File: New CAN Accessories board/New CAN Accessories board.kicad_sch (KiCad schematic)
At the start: 85 parts, among them J1 39301040, J10 39301040, J11 ATF13-2P-BM03, J2 39301040, J3 39301040, J4 39301040, J5 39301040, J6 39301040, J7 39301040, J8 39301040, J9 39301060, Q1 IRLML6344TRPBF, Q2 IRLML6344TRPBF, Q3 IRLML6344TRPBF, Q4 IRLML6344TRPBF, Q5 IRLML6344TRPBF, Q6 IRLML6344TRPBF, Q7 IRLML6344TRPBF, Q8 IRLML6344TRPBF, T1 MCP2562FD-E_SN, U1 NUCLEO_L432KC

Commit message: Annotate
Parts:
- renumbered Rterm to Rterm1, SWsel to SWsel1, SWtel to SWtel1
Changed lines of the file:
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@@
 		(on_board yes)
 		(dnp no)
-		(property "Reference" "Rterm"
+		(property "Reference" "Rterm1"
 			(at 44.958 144.8816 0)
 			(effects
@@
 			(project "New CAN Accessories board"
 				(path "/88340f43-3f46-45a6-9393-130e00dc3071"
-					(reference "Rterm")
+					(reference "Rterm1")
 					(unit 1)
 				)
@@
 		(dnp no)
 		(fields_autoplaced yes)
-		(property "Reference" "SWsel"
+		(property "Reference" "SWsel1"
 			(at 49.53 190.5 0)
 			(effects
@@
 			(project "New CAN Accessories board"
 				(path "/88340f43-3f46-45a6-9393-130e00dc3071"
-					(reference "SWsel")
+					(reference "SWsel1")
 					(unit 2)
 				)
@@
 		(dnp no)
 		(fields_autoplaced yes)
-		(property "Reference" "SWsel"
+		(property "Reference" "SWsel1"
 			(at 49.53 181.61 0)
 			(effects
@@
 			(project ""
 				(path "/88340f43-3f46-45a6-9393-130e00dc3071"
-					(reference "SWsel")
+					(reference "SWsel1")
 					(unit 1)
 				)
@@
 		(dnp no)
 		(fields_autoplaced yes)
-		(property "Reference" "SWtel"
+		(property "Reference" "SWtel1"
 			(at 87.63 190.5 0)
 			(effects
@@
 			(project "New CAN Accessories board"
 				(path "/88340f43-3f46-45a6-9393-130e00dc3071"
-					(reference "SWtel")
+					(reference "SWtel1")
 					(unit 2)
 				)
@@
 		(dnp no)
 		(fields_autoplaced yes)
-		(property "Reference" "SWtel"
+		(property "Reference" "SWtel1"
 			(at 87.63 181.61 0)
 			(effects
@@
 			(project "New CAN Accessories board"
 				(path "/88340f43-3f46-45a6-9393-130e00dc3071"
-					(reference "SWtel")
+					(reference "SWtel1")
 					(unit 1)
 				)

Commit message: preliminary layout complete
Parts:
- removed Cop1, Cop2, Cop3, Cop4, Cop5, Cop6, Cop7, Cop8: 100nF, Capacitor_SMD:C_0805_2012Metric, symbol Device:C
- removed D1, D2, D3, D4, D5, D6, D7, D8: LED, LED_SMD:LED_0805_2012Metric, symbol Device:LED
- removed F1, F2, F3, F4, F5, F6, F7, F8: Fuse, footprint:3586KTR, symbol Device:Fuse
- removed J1, J2, J3, J4, J5, J6, J7, J8: 39301040, Connector_Molex:Molex_Mini-Fit_Jr_5569-04A2_2x02_P4.20mm_Horizontal, symbol Connector_Generic:Conn_02x02_Top_Bottom
- removed OP1, OP2, OP3, OP4, OP5, OP6, OP7, OP8: MCP6C02T-020E/CHY, footprint:SOT-23-6_CHY_MCH-M, symbol sym:MCP6C02T-020E_CHY
- removed Q1, Q2, Q3, Q4, Q5, Q6, Q7, Q8: IRLML6344TRPBF, footprint:TRANS_IRLML6344TRPBF, symbol sym:IRLML6344TRPBF
- removed Rled1, Rled2, Rled3, Rled4, Rled5, Rled6, Rled7, Rled8: 100, Resistor_SMD:R_0805_2012Metric, symbol Device:R
- removed Rpd1, Rpd2, Rpd3, Rpd4, Rpd5, Rpd6, Rpd7, Rpd8: 10K, Resistor_SMD:R_0805_2012Metric, symbol Device:R
- removed Rsh1, Rsh2, Rsh3, Rsh4, Rsh5, Rsh6, Rsh7, Rsh8: 0.05, Resistor_SMD:R_2512_6332Metric_Pad1.40x3.35mm_HandSolder, symbol Device:R
- Rpd10, SWtel1: now not fitted
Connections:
- net BOARD_SW: now also SWsel1.6 (C), U1.PB3 (D13); no longer SWsel1.4 (A), U1.PB0 (D3)
- net CANRX: now also U1.PA9 (D1); no longer U1.PA11 (D10)
- net GATE1: now also U1.PB4 (D12); no longer U1.PB1 (D6)
- net GATE2: now also U1.PB5 (D11); no longer U1.PA8 (D9)
- net GATE3: now also U1.PA8 (D9); no longer U1.PB7 (D4)
- net GATE4: now also U1.PB1 (D6); no longer U1.PB6 (D5)
- net GATE5: now also U1.PB6 (D5); no longer U1.PB5 (D11)
- net GATE6: now also U1.PB7 (D4); no longer U1.PB4 (D12)
- net GATE7: now also U1.PB0 (D3)
- net GATE8: now also U1.PA10 (D0)
- net STBY: now also U1.PA11 (D10); no longer U1.PA9 (D1)
- net TELEM_SW: no longer U1.PB3 (D13)
- no-connect marks 10 -> 9
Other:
- added sheet M1 (Module.kicad_sch)
- added sheet M2 (Module.kicad_sch)
- added sheet M3 (Module.kicad_sch)
- added sheet M4 (Module.kicad_sch)
- added sheet M5 (Module.kicad_sch)
- added sheet M6 (Module.kicad_sch)
- added sheet M7 (Module.kicad_sch)
- added sheet M8 (Module.kicad_sch)

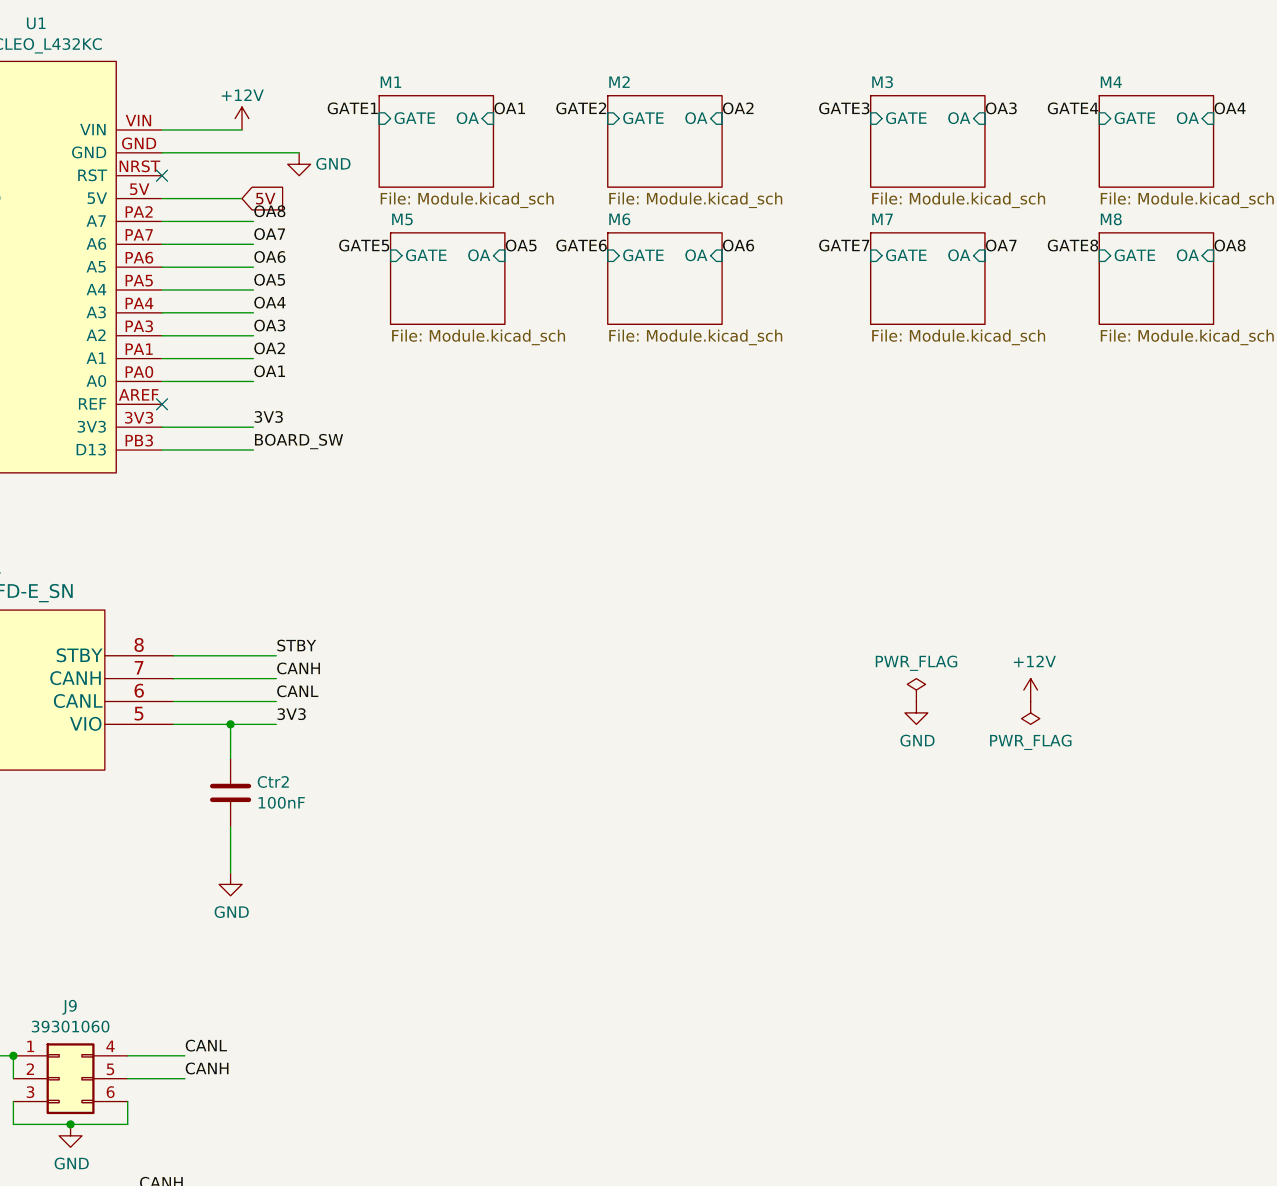
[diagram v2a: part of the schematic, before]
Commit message: added test points in schematic
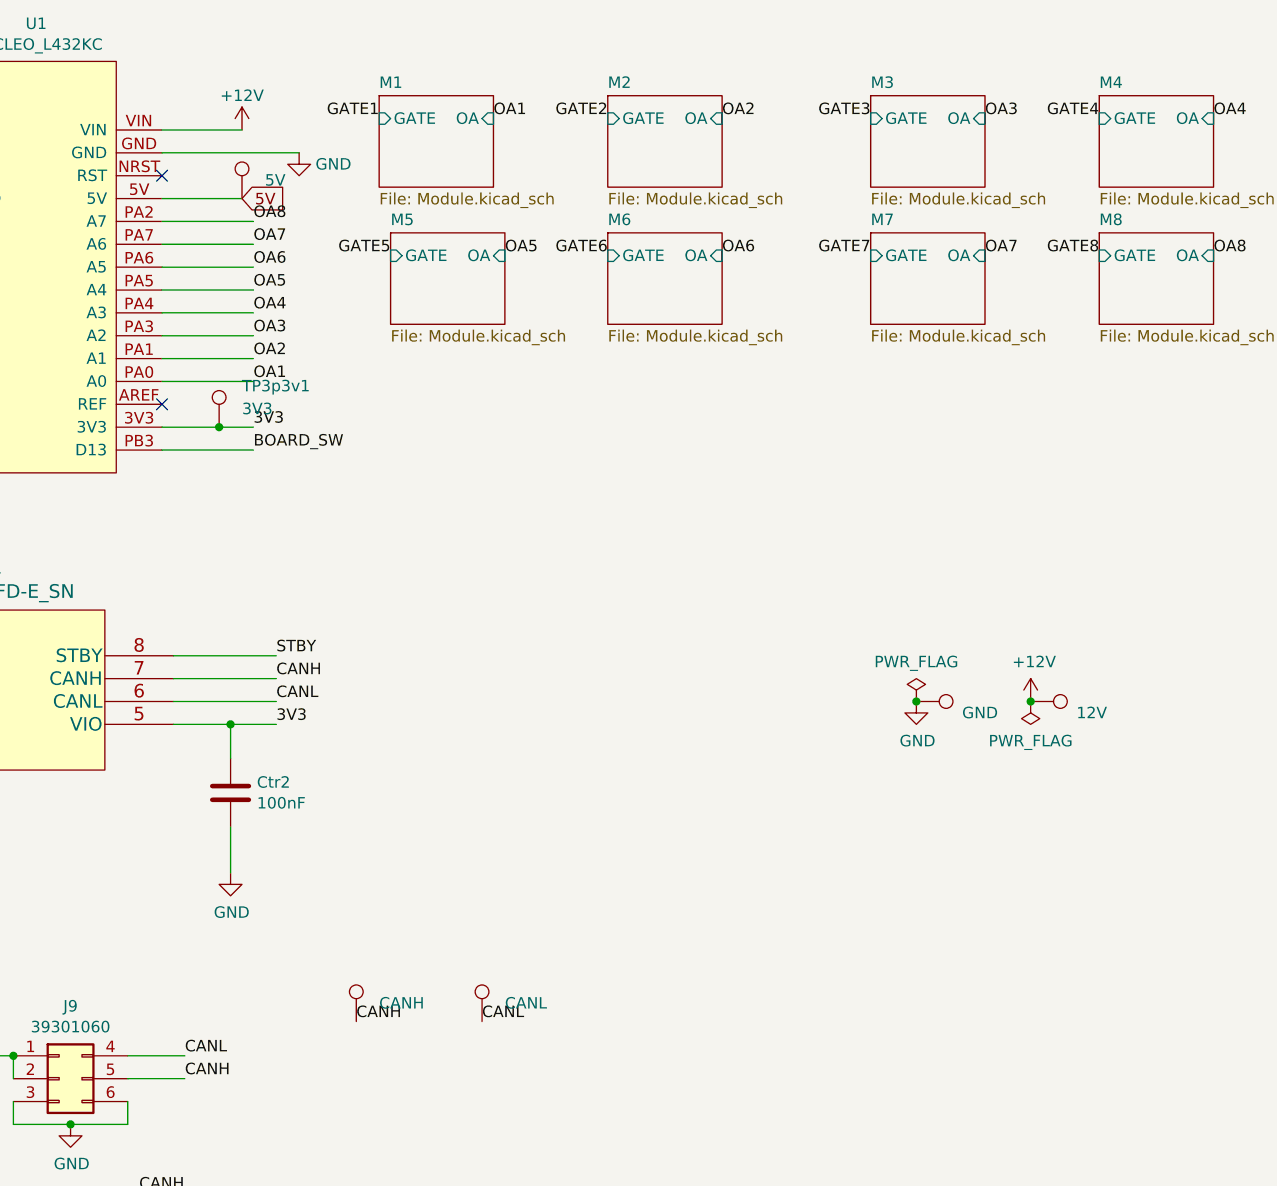
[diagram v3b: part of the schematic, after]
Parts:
- added TP12v1: 12V, Connector_PinHeader_1.00mm:PinHeader_1x01_P1.00mm_Vertical, symbol Connector:TestPoint
- added TP3p3v1: 3V3, Connector_PinHeader_1.00mm:PinHeader_1x01_P1.00mm_Vertical, symbol Connector:TestPoint
- added TP5v1: 5V, Connector_PinHeader_1.00mm:PinHeader_1x01_P1.00mm_Vertical, symbol Connector:TestPoint
- added TPcanh1: CANH, Connector_PinHeader_1.00mm:PinHeader_1x01_P1.00mm_Vertical, symbol Connector:TestPoint
- added TPcanl1: CANL, Connector_PinHeader_1.00mm:PinHeader_1x01_P1.00mm_Vertical, symbol Connector:TestPoint
- added TPgnd1: GND, Connector_PinHeader_1.00mm:PinHeader_1x01_P1.00mm_Vertical, symbol Connector:TestPoint
- T1: footprint footprint:MCP2562FD-E_SN -> Package_SO:SOIC-8_3.9x4.9mm_P1.27mm
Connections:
- net +12V: now also TP12v1.1
- net 3V3: now also TP3p3v1.1
- net 5V: now also TP5v1.1
- net CANH: now also TPcanh1.1
- net CANL: now also TPcanl1.1
- net GND: now also TPgnd1.1

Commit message: post design review
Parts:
- removed TPcanh1: CANH, Connector_PinHeader_1.00mm:PinHeader_1x01_P1.00mm_Vertical, symbol Connector:TestPoint
- removed TPcanl1: CANL, Connector_PinHeader_1.00mm:PinHeader_1x01_P1.00mm_Vertical, symbol Connector:TestPoint
- added H1, H2, H3: MountingHole, MountingHole:MountingHole_3.2mm_M3_ISO14580, symbol Mechanical:MountingHole
- added J12: Conn_01x02_Pin, Connector_PinHeader_2.54mm:PinHeader_1x02_P2.54mm_Vertical, symbol Connector:Conn_01x02_Pin
- renumbered JP4 to JP1
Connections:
- net CANH: now also J12.1 (Pin_1)
- net CANL: now also J12.2 (Pin_2)
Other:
- moved on the sheet: J10, J11, J9, JP1, Rpd10, Rpd9, Rterm1, SWsel1A, SWsel1B, SWtel1A, SWtel1B

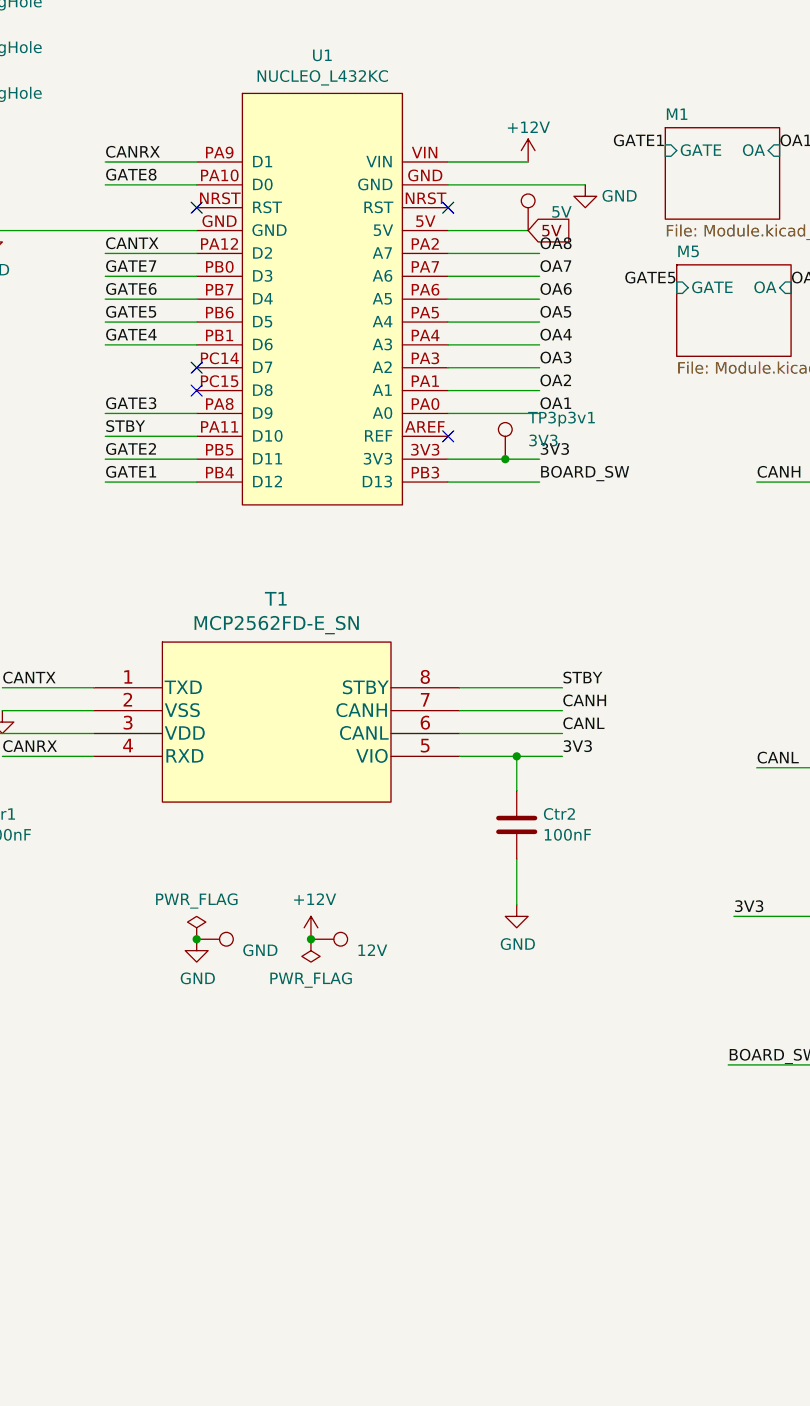
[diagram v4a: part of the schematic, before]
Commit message: Added test points 1x12 pin and 1x8 pin
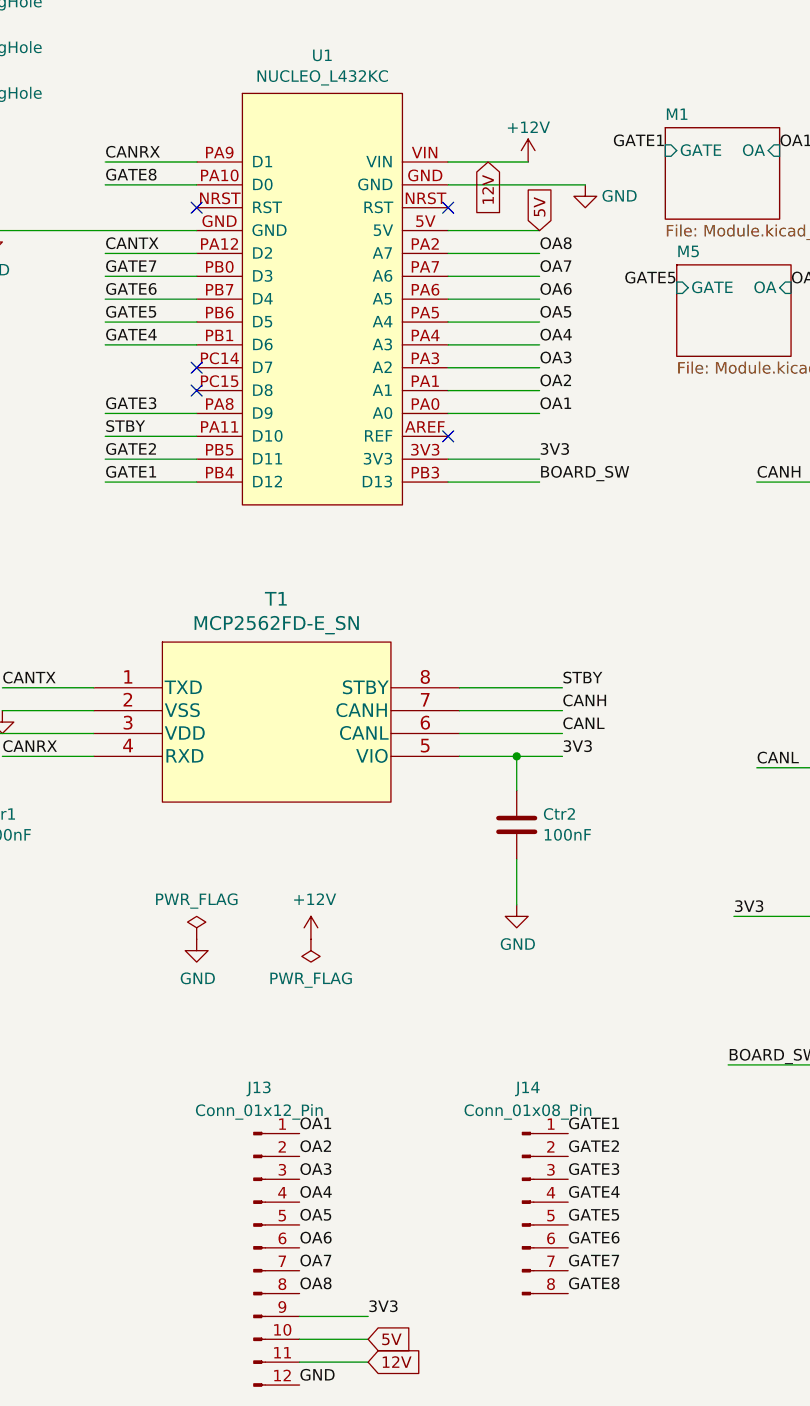
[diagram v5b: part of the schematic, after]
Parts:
- removed TP12v1: 12V, Connector_PinHeader_1.00mm:PinHeader_1x01_P1.00mm_Vertical, symbol Connector:TestPoint
- removed TP3p3v1: 3V3, Connector_PinHeader_1.00mm:PinHeader_1x01_P1.00mm_Vertical, symbol Connector:TestPoint
- removed TP5v1: 5V, Connector_PinHeader_1.00mm:PinHeader_1x01_P1.00mm_Vertical, symbol Connector:TestPoint
- removed TPgnd1: GND, Connector_PinHeader_1.00mm:PinHeader_1x01_P1.00mm_Vertical, symbol Connector:TestPoint
- added J13: Conn_01x12_Pin, Connector_PinHeader_2.54mm:PinHeader_1x12_P2.54mm_Vertical, symbol Connector:Conn_01x12_Pin
- added J14: Conn_01x08_Pin, Connector_PinHeader_2.54mm:PinHeader_1x08_P2.54mm_Vertical, symbol Connector:Conn_01x08_Pin
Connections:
- net +12V: now also J13.11 (Pin_11)
- net 3V3: now also J13.9 (Pin_9)
- net 5V: now also J13.10 (Pin_10)
- net GATE1: now also J14.1 (Pin_1)
- net GATE2: now also J14.2 (Pin_2)
- net GATE3: now also J14.3 (Pin_3)
- net GATE4: now also J14.4 (Pin_4)
- net GATE5: now also J14.5 (Pin_5)
- net GATE6: now also J14.6 (Pin_6)
- net GATE7: now also J14.7 (Pin_7)
- net GATE8: now also J14.8 (Pin_8)
- net GND: now also J13.12 (Pin_12)
- net OA1: now also J13.1 (Pin_1)
- net OA2: now also J13.2 (Pin_2)
- net OA3: now also J13.3 (Pin_3)
- net OA4: now also J13.4 (Pin_4)
- net OA5: now also J13.5 (Pin_5)
- net OA6: now also J13.6 (Pin_6)
- net OA7: now also J13.7 (Pin_7)
- net OA8: now also J13.8 (Pin_8)
